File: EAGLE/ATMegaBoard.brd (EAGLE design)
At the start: 71.1 x 54.3 mm, 30 parts, among them IC1 L298, IC2 ATMEGA168-20P, IC3 REG1117, X1 49S/18PF

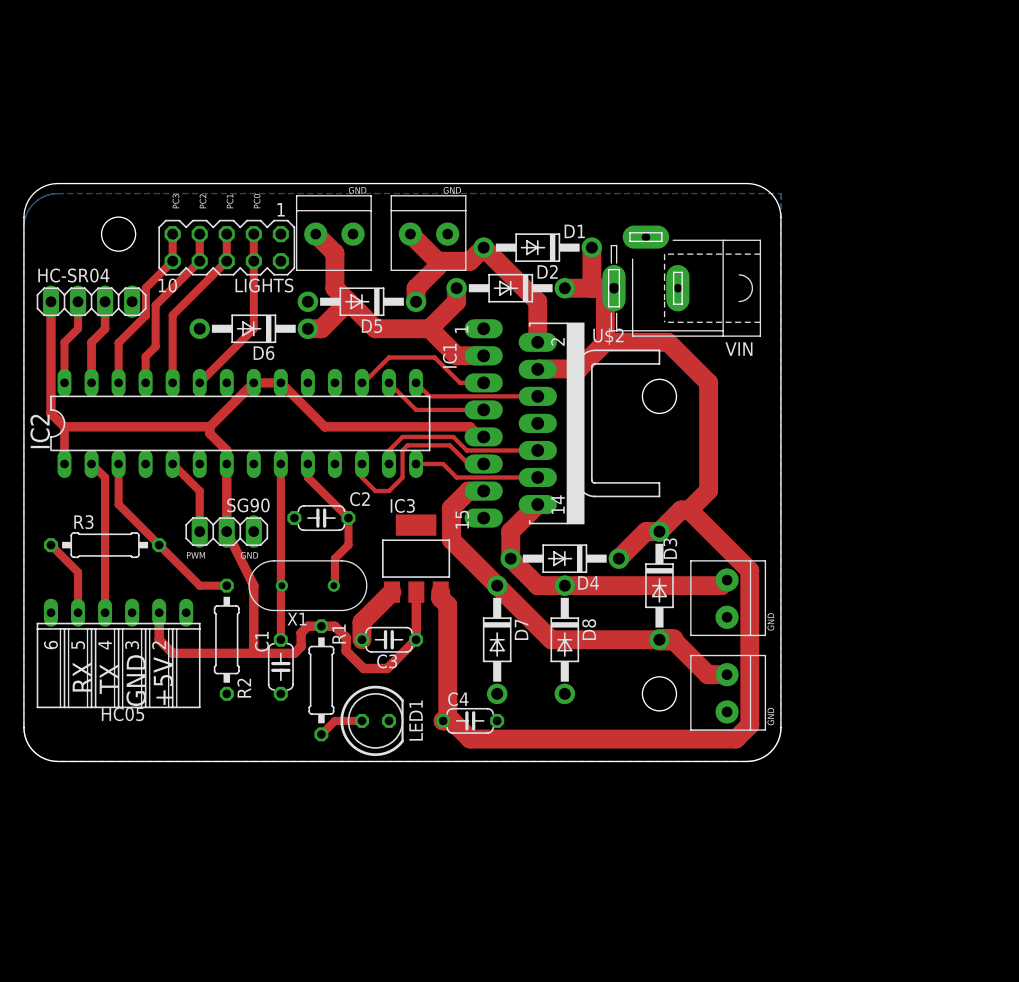
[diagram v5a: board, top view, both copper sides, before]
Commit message: updated board to change mounted orientation
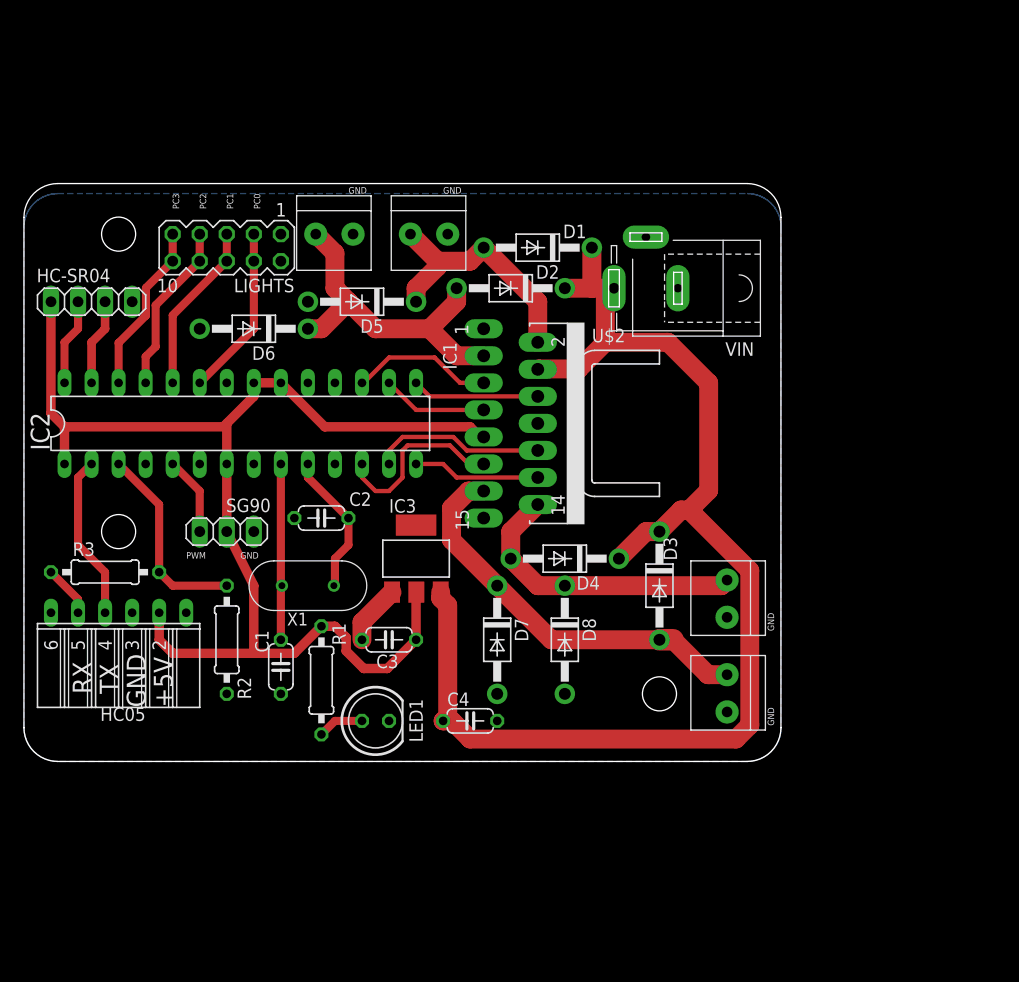
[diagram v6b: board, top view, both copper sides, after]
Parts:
- moved R3 2.54 mm to (7.62, 17.8)
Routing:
- net PIN5HC05: track 7.40 -> 4.86 mm
- net RX: track 17.1 -> 18.6 mm
- net TX: track 14.5 -> 15.5 mm
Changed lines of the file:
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@@
 <drawing>
 <settings>
-<setting alwaysvectorfont="no"/>
+<setting alwaysvectorfont="yes"/>
 <setting verticaltext="up"/>
 </settings>
@@
 <wire x1="67.925" y1="54.28" x2="3.175" y2="54.28" width="0" layer="20"/>
 <wire x1="3.175" y1="54.28" x2="0" y2="51.105" width="0" layer="20" curve="90"/>
+<hole x="59.69" y="6.35" drill="3.19999375"/>
+<hole x="8.89" y="21.59" drill="3.19999375"/>
 <hole x="8.89" y="49.53" drill="3.19999375"/>
-<hole x="59.69" y="34.29" drill="3.19999375"/>
-<hole x="59.69" y="6.35" drill="3.19999375"/>
 <text x="15.24" y="19.05" size="0.6096" layer="21">PWM</text>
 <text x="20.32" y="19.05" size="0.6096" layer="21">GND</text>
@@
 </variantdefs>
 <classes>
-<class number="0" name="default" width="0" drill="0">
+<class number="0" name="default" width="0.3048" drill="0">
 </class>
 <class number="1" name="Power" width="1.778" drill="0">
 </class>
-<class number="2" name="5v" width="0.762" drill="0">
+<class number="2" name="5v" width="0.889" drill="0">
 </class>
 </classes>
@@
 <attribute name="VALUE" x="19.685" y="9.1694" size="1.27" layer="27" ratio="10" rot="R90"/>
 </element>
-<element name="R3" library="rcl" library_urn="urn:adsk.eagle:library:334" package="0207/10" package3d_urn="urn:adsk.eagle:package:23491/2" value="1k" x="7.62" y="20.32" smashed="yes">
-<attribute name="NAME" x="4.572" y="21.844" size="1.27" layer="25" ratio="10"/>
-<attribute name="POPULARITY" value="36" x="7.62" y="20.32" size="1.778" layer="27" display="off"/>
-<attribute name="SPICEPREFIX" value="R" x="7.62" y="20.32" size="1.778" layer="27" display="off"/>
-<attribute name="VALUE" x="5.3594" y="19.685" size="1.27" layer="27" ratio="10"/>
+<element name="R3" library="rcl" library_urn="urn:adsk.eagle:library:334" package="0207/10" package3d_urn="urn:adsk.eagle:package:23491/2" value="1k" x="7.62" y="17.78" smashed="yes">
+<attribute name="NAME" x="4.572" y="19.304" size="1.27" layer="25" ratio="10"/>
+<attribute name="POPULARITY" value="36" x="7.62" y="17.78" size="1.778" layer="27" display="off"/>
+<attribute name="SPICEPREFIX" value="R" x="7.62" y="17.78" size="1.778" layer="27" display="off"/>
+<attribute name="VALUE" x="5.3594" y="17.145" size="1.27" layer="27" ratio="10"/>
 </element>
 <element name="U$2" library="heatsink" library_urn="urn:adsk.eagle:library:236" package="D03S" package3d_urn="urn:adsk.eagle:package:14190/1" value="" x="53.34" y="31.75" smashed="yes" rot="R270">
@@
 <contactref element="R3" pad="2"/>
 <contactref element="R2" pad="2"/>
-<wire x1="19.05" y1="16.51" x2="16.51" y2="16.51" width="0.762" layer="1"/>
-<wire x1="16.51" y1="16.51" x2="12.7" y2="20.32" width="0.762" layer="1"/>
-<wire x1="12.7" y1="20.32" x2="8.89" y2="24.13" width="0.762" layer="1"/>
-<wire x1="8.89" y1="27.94" x2="8.89" y2="24.13" width="0.762" layer="1"/>
+<wire x1="19.05" y1="16.51" x2="13.97" y2="16.51" width="0.762" layer="1"/>
+<wire x1="13.97" y1="16.51" x2="12.7" y2="17.78" width="0.762" layer="1"/>
+<wire x1="12.7" y1="17.78" x2="12.7" y2="24.13" width="0.762" layer="1"/>
+<wire x1="12.7" y1="24.13" x2="8.89" y2="27.94" width="0.762" layer="1"/>
 </signal>
 <signal name="TX">
 <contactref element="IC2" pad="2"/>
 <contactref element="HC05" pad="4"/>
-<wire x1="6.35" y1="27.94" x2="7.62" y2="26.67" width="0.762" layer="1"/>
-<wire x1="7.62" y1="26.67" x2="7.62" y2="13.97" width="0.762" layer="1"/>
+<wire x1="6.35" y1="27.94" x2="5.08" y2="26.67" width="0.762" layer="1"/>
+<wire x1="5.08" y1="26.67" x2="5.08" y2="20.32" width="0.762" layer="1"/>
+<wire x1="7.62" y1="17.78" x2="7.62" y2="13.97" width="0.762" layer="1"/>
+<wire x1="7.62" y1="17.78" x2="5.08" y2="20.32" width="0.762" layer="1"/>
 </signal>
 <signal name="+5V" class="2">
@@
 <contactref element="C3" pad="1"/>
 <contactref element="R1" pad="2"/>
-<wire x1="36.83" y1="11.43" x2="34.13125" y2="8.73125" width="0.889" layer="1"/>
 <wire x1="19.05" y1="21.59" x2="19.05" y2="27.94" width="0.889" layer="1"/>
 <wire x1="19.05" y1="21.59" x2="21.59" y2="16.51" width="0.889" layer="1"/>
-<wire x1="19.05" y1="27.94" x2="19.05" y2="29.21" width="0.889" layer="1"/>
 <wire x1="21.59" y1="10.16" x2="13.97" y2="10.16" width="0.889" layer="1"/>
 <wire x1="21.59" y1="10.16" x2="25.4" y2="10.16" width="0.889" layer="1"/>
-<wire x1="26.035" y1="10.795" x2="25.4" y2="10.16" width="0.889" layer="1"/>
 <wire x1="2.54" y1="32.7025" x2="2.54" y2="43.18" width="0.889" layer="1"/>
-<wire x1="36.83" y1="11.43" x2="36.8554" y2="11.4554" width="0.762" layer="1"/>
-<wire x1="36.8554" y1="15.9004" x2="36.8554" y2="11.4554" width="0.889" layer="1"/>
 <contactref element="HC05" pad="2"/>
 <wire x1="12.7" y1="11.43" x2="12.7" y2="13.97" width="0.889" layer="1"/>
@@
 <wire x1="2.54" y1="32.7025" x2="3.81" y2="31.4325" width="0.889" layer="1"/>
 <contactref element="IC2" pad="1"/>
-<wire x1="3.81" y1="31.4325" x2="3.81" y2="27.94" width="0.8128" layer="1"/>
 <wire x1="43.18" y1="30.48" x2="42.8625" y2="30.48" width="0.889" layer="1"/>
 <wire x1="41.91" y1="31.4325" x2="42.8625" y2="30.48" width="0.889" layer="1"/>
-<wire x1="34.13125" y1="8.73125" x2="31.90875" y2="8.73125" width="0.889" layer="1"/>
+<wire x1="31.90875" y1="8.73125" x2="34.13125" y2="8.73125" width="0.889" layer="1"/>
 <wire x1="31.90875" y1="8.73125" x2="30.2641" y2="10.3759" width="0.889" layer="1"/>
 <wire x1="30.2641" y1="11.6459" x2="29.21" y2="12.7" width="0.889" layer="1"/>
 <wire x1="29.21" y1="12.7" x2="27.94" y2="12.7" width="0.889" layer="1"/>
 <wire x1="30.2641" y1="10.3759" x2="30.2641" y2="11.6459" width="0.889" layer="1"/>
-<wire x1="27.94" y1="12.7" x2="26.67" y2="12.7" width="0.889" layer="1"/>
-<wire x1="26.67" y1="12.7" x2="26.035" y2="12.065" width="0.889" layer="1"/>
-<wire x1="26.035" y1="12.065" x2="26.035" y2="10.795" width="0.889" layer="1"/>
+<wire x1="27.94" y1="12.7" x2="25.4" y2="10.16" width="0.889" layer="1"/>
 <wire x1="13.97" y1="10.16" x2="12.7" y2="11.43" width="0.889" layer="1"/>
-<wire x1="3.81" y1="31.4325" x2="17.4625" y2="31.4325" width="0.889" layer="1"/>
-<wire x1="17.4625" y1="31.4325" x2="21.59" y2="35.56" width="0.889" layer="1"/>
 <wire x1="21.59" y1="35.56" x2="24.13" y2="35.56" width="0.889" layer="1"/>
 <wire x1="24.13" y1="35.56" x2="28.2575" y2="31.4325" width="0.889" layer="1"/>
 <wire x1="28.2575" y1="31.4325" x2="41.91" y2="31.4325" width="0.889" layer="1"/>
-<wire x1="19.05" y1="29.21" x2="17.4625" y2="30.7975" width="0.889" layer="1"/>
-<wire x1="17.4625" y1="30.7975" x2="17.4625" y2="31.4325" width="0.889" layer="1"/>
+<wire x1="19.05" y1="31.75" x2="21.59" y2="34.29" width="0.889" layer="1"/>
+<wire x1="21.59" y1="34.29" x2="21.59" y2="35.56" width="0.889" layer="1"/>
+<wire x1="19.05" y1="27.94" x2="19.05" y2="31.75" width="0.889" layer="1"/>
+<wire x1="18.7325" y1="31.4325" x2="19.05" y2="31.75" width="0.889" layer="1"/>
+<wire x1="3.81" y1="31.4325" x2="18.7325" y2="31.4325" width="0.889" layer="1"/>
+<wire x1="34.13125" y1="8.73125" x2="36.83" y2="11.43" width="0.889" layer="1"/>
+<wire x1="36.83" y1="11.43" x2="36.83" y2="15.875" width="0.889" layer="1"/>
+<wire x1="36.83" y1="15.875" x2="36.8554" y2="15.9004" width="0.889" layer="1"/>
+<wire x1="3.81" y1="27.94" x2="3.81" y2="31.4325" width="0.889" layer="1"/>
 </signal>
 <signal name="GND" class="1">
@@
 <contactref element="C4" pad="2"/>
 <contactref element="R2" pad="1"/>
-<polygon width="0.635" layer="16">
+<polygon width="0.508" layer="16">
 <vertex x="0" y="3.175"/>
 <vertex x="0" y="50.165" curve="-90"/>
 <vertex x="3.175" y="53.34"/>
-<vertex x="71.12" y="53.34"/>
+<vertex x="67.945" y="53.34" curve="-90"/>
+<vertex x="71.12" y="50.165"/>
 <vertex x="71.12" y="3.175" curve="-90"/>
 <vertex x="67.945" y="0"/>
@@
 <contactref element="HC05" pad="5"/>
 <contactref element="R3" pad="1"/>
-<wire x1="5.08" y1="17.78" x2="5.08" y2="13.97" width="0.762" layer="1"/>
-<wire x1="5.08" y1="17.78" x2="2.54" y2="20.32" width="0.762" layer="1"/>
+<wire x1="5.08" y1="15.24" x2="5.08" y2="13.97" width="0.762" layer="1"/>
+<wire x1="5.08" y1="15.24" x2="2.54" y2="17.78" width="0.762" layer="1"/>
 </signal>
 <signal name="N$1">

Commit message: updated output for LEDs
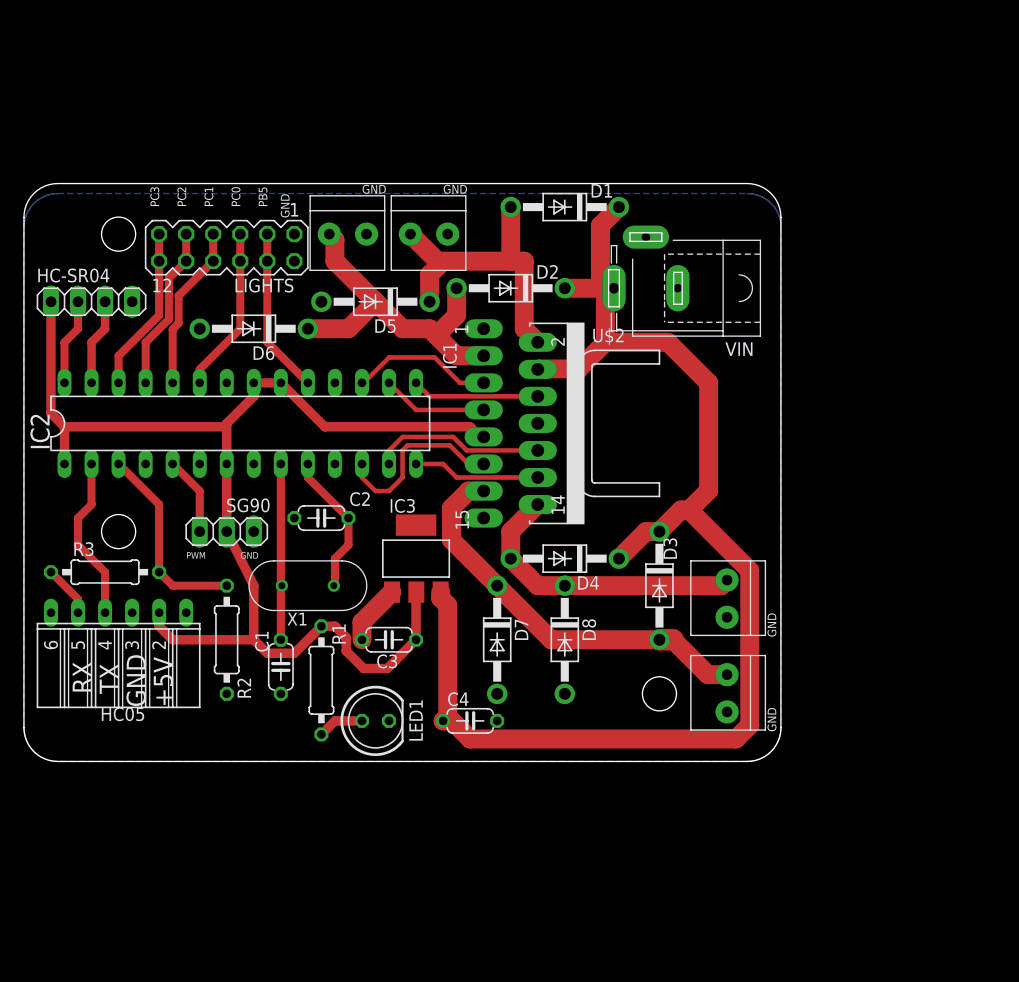
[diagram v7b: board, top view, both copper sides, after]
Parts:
- LIGHTS: device con-lstb:MA05-2 -> con-lstb:MA06-2
- moved D1 4.58 mm to (50.8, 52.1)
- moved D5 1.27 mm to (33.0, 43.2)
- moved OUT2 1.27 mm to (30.5, 49.5)
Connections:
- new net N$7: IC2.26, LIGHTS.11, LIGHTS.12
- net N$1: now also IC2.19; no longer IC2.23
- net N$2: now also IC2.23; no longer IC2.24
- net N$4: now also IC2.24; no longer IC2.25
- net N$5: now also IC2.25; no longer IC2.26
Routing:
- net N$7: track 0.00 -> 15.5 mm
- net VIN: track 118.5 -> 124.3 mm
- net OUT1: track 24.1 -> 29.1 mm
- net +5V: track 118.1 -> 116.1 mm
- net OUT2: track 32.2 -> 33.0 mm
- net N$4: track 16.1 -> 15.5 mm
- net N$5: track 16.1 -> 15.5 mm
- net N$2: track 16.1 -> 15.5 mm
- net N$1: track 16.1 -> 15.5 mm
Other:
- board text added: "PB5"

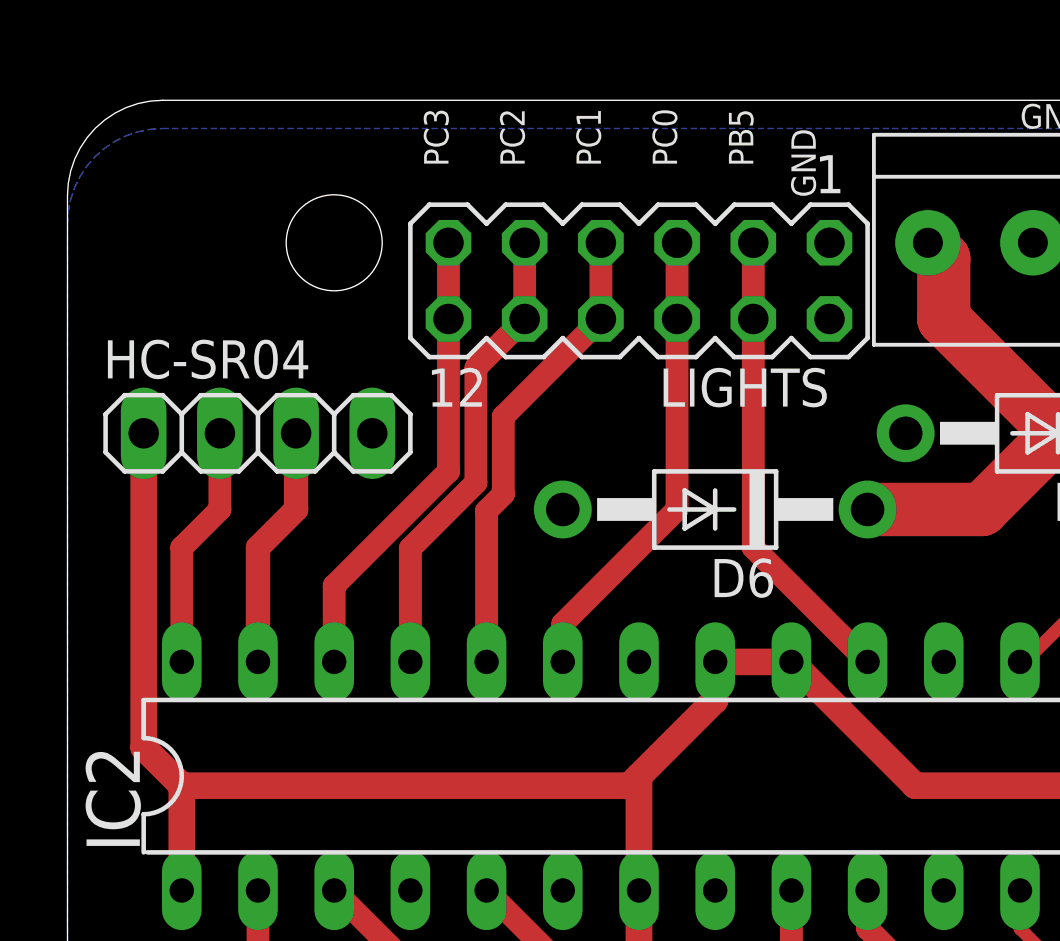
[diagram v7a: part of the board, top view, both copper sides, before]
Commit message: expanded LED lighting to be 1 to 1
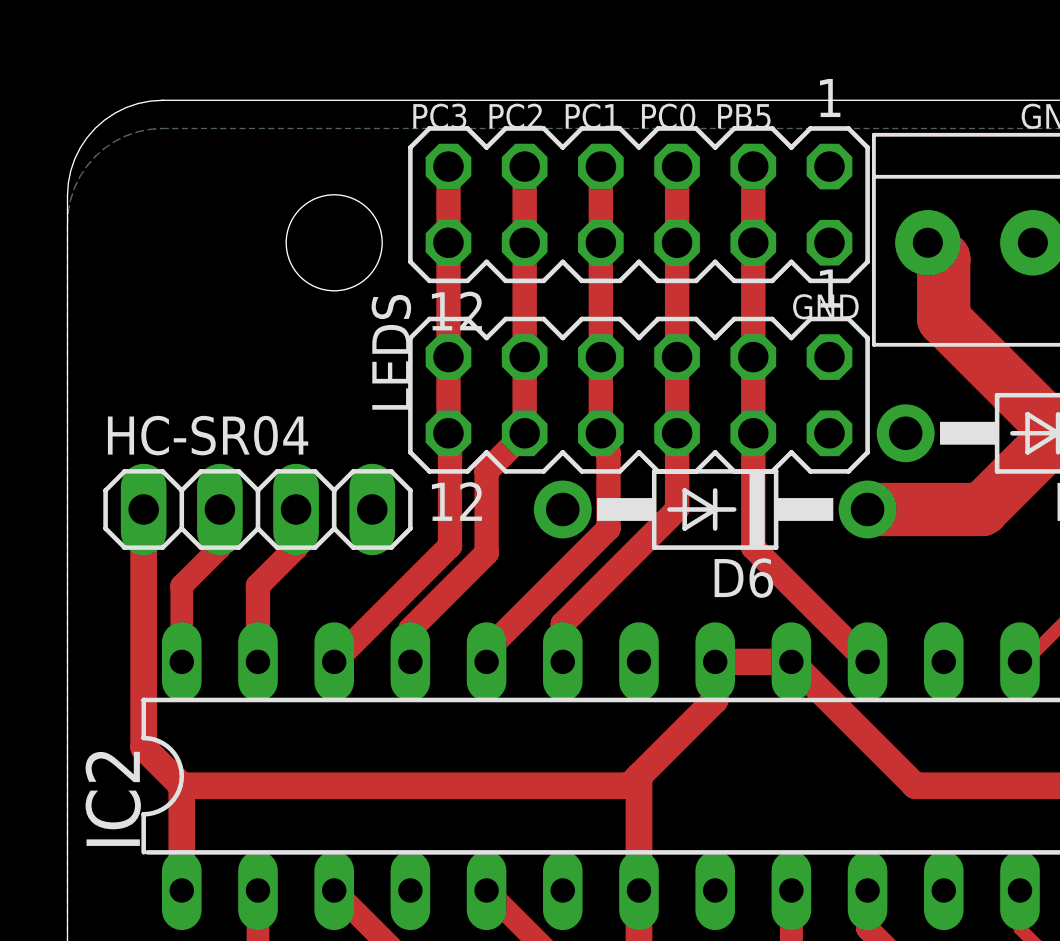
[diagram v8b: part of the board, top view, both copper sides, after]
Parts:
- removed LIGHTS: (no value), con-lstb:MA06-2
- added LEDS, LIGHTS1: (no value), con-lstb:MA06-2
- moved HC-SR04 2.54 mm to (6.35, 40.6)
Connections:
- removed net N$1: IC2.19, LIGHTS.3, LIGHTS.4
- new net N$6: IC2.19, LEDS.3, LEDS.4, LIGHTS1.3, LIGHTS1.4
- net GND: now also LEDS.1, LEDS.2, LIGHTS1.1, LIGHTS1.2; no longer LIGHTS.1, LIGHTS.2
- net N$2: now also LEDS.5, LEDS.6, LIGHTS1.5, LIGHTS1.6; no longer LIGHTS.5, LIGHTS.6
- net N$4: now also LEDS.7, LEDS.8, LIGHTS1.7, LIGHTS1.8; no longer LIGHTS.7, LIGHTS.8
- net N$5: now also LEDS.10, LEDS.9, LIGHTS1.10, LIGHTS1.9; no longer LIGHTS.10, LIGHTS.9
- net N$7: now also LEDS.11, LEDS.12, LIGHTS1.11, LIGHTS1.12; no longer LIGHTS.11, LIGHTS.12
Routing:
- net N$6: track 0.00 -> 18.1 mm
- net N$1: track 15.5 -> 0.00 mm
- net N$4: track 15.5 -> 18.3 mm
- net N$7: track 15.5 -> 18.1 mm
- net +5V: track 116.1 -> 113.6 mm
- net N$5: track 15.5 -> 18.1 mm
- net N$2: track 15.5 -> 18.1 mm
- net TRIG: track 8.15 -> 5.61 mm
- net ECHO: track 8.15 -> 5.61 mm
